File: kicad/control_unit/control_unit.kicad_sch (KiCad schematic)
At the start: 16 parts

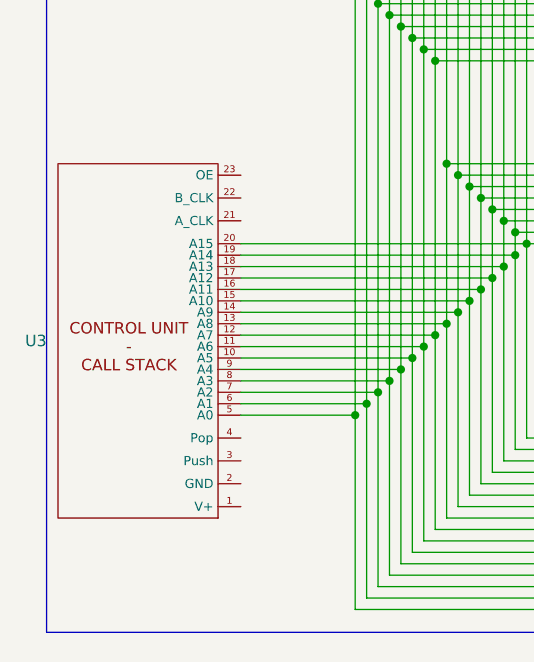
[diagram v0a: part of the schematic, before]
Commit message: Work on call stack and instruction sequence timing
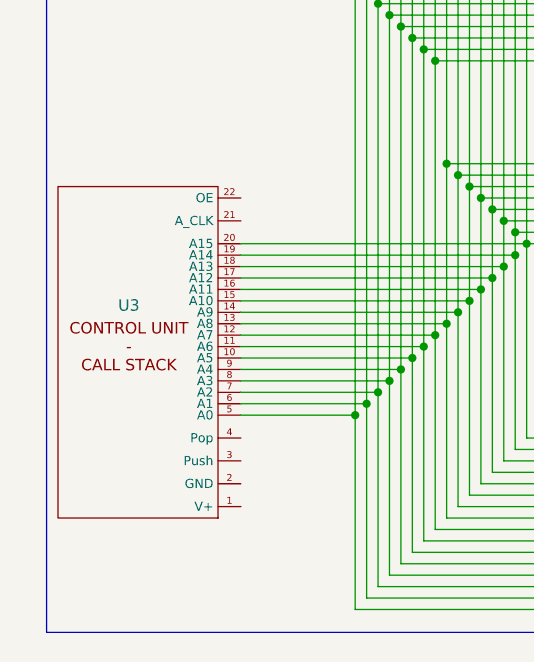
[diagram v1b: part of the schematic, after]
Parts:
- U3: value ~ -> (none); footprint Connector_PinHeader_2.54mm:PinHeader_1x23_P2.54mm_Vertical -> Connector_PinHeader_2.54mm:PinHeader_1x22_P2.54mm_Vertical
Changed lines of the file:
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@@
 		(dnp no)
 		(property "Reference" "U3"
-			(at 138.43 269.8751 0)
+			(at 147.574 265.938 0)
 			(effects
 				(font
 					(size 1.27 1.27)
 				)
-				(justify left)
 			)
 		)
-		(property "Value" "~"
+		(property "Value" ""
 			(at 157.48 275.59 0)
 			(effects
@@
 			)
 		)
-		(property "Footprint" "Connector_PinHeader_2.54mm:PinHeader_1x23_P2.54mm_Vertical"
-			(at 148.336 247.142 0)
+		(property "Footprint" "Connector_PinHeader_2.54mm:PinHeader_1x22_P2.54mm_Vertical"
+			(at 148.336 250.952 0)
 			(effects
 				(font
@@
 		(pin "15"
 		)
-		(pin "23"
-		)
 		(instances

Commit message: Finished startup controller
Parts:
- removed U4: ~, Connector_PinHeader_2.54mm:PinHeader_1x39_P2.54mm_Vertical, symbol custom_symbol_lib:prog_mem_interface
- added D1, D2, D3, D4: LED, LED_THT:LED_D4.0mm, symbol Device:LED
- added R2, R3, R5, R6, R7: 10k, custom_footprint_library:0.4_pitch_resistor, symbol Device:R
- added U11: ~, Connector_PinHeader_2.54mm:PinHeader_1x23_P2.54mm_Horizontal, symbol custom_symbol_lib:control_unit_central_timing_interface
- added U12, U16: ~, Package_DIP:DIP-14_W7.62mm, symbol custom_symbol_lib:quad_and
- added U14: ~, Package_DIP:DIP-14_W7.62mm, symbol custom_symbol_lib:quad_OR
- added U17: ~, Connector_PinHeader_2.54mm:PinHeader_1x40_P2.54mm_Vertical, symbol custom_symbol_lib:prog_mem_interface
- added U20: ~, Package_DIP:DIP-14_W7.62mm, symbol custom_symbol_lib:6xNOT
- added U22: ~, Connector_PinHeader_2.54mm:PinHeader_1x04_P2.54mm_Vertical, symbol custom_symbol_lib:ALU_opcode
- added U23, U25: ~, custom_footprint_library:jumper, symbol custom_symbol_lib:jumper
- added U4: ~, Package_DIP:DIP-14_W7.62mm, symbol custom_symbol_lib:dual_latch
- U1: footprint Connector_PinHeader_2.54mm:PinHeader_1x22_P2.54mm_Vertical -> Connector_PinHeader_2.54mm:PinHeader_1x23_P2.54mm_Vertical
- U2: footprint Connector_PinHeader_2.54mm:PinHeader_1x10_P2.54mm_Vertical -> Connector_PinHeader_2.54mm:PinHeader_1x11_P2.54mm_Vertical
- U3: value (none) -> ~; footprint Connector_PinHeader_2.54mm:PinHeader_1x22_P2.54mm_Vertical -> Connector_PinHeader_2.54mm:PinHeader_1x24_P2.54mm_Vertical
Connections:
- net at U5.1 (OE#): now also U7.1 (OE#), U20.10 (O4)
- net at U5.10 (GND): now also U1.13 (GND), U10.10 (B2), U10.13 (B3), U10.15 (OE#), U10.8 (GND), U13.11 (B3), U13.15 (B2), U13.2 (B1), U13.6 (B0), U13.8 (GND), U15.8 (GND), U18.11 (B3), U18.15 (B2), U18.2 (B1), U18.6 (B0), U18.8 (GND), U19.10 (GND), U21.11 (B3), U21.15 (B2), U21.2 (B1), U21.7 (C_IN), U21.8 (GND), U24.10 (GND), U3.2 (GND), U6.1 (OE#), U6.10 (GND), U7.10 (GND), U8.10 (GND), U9.1 (OE#), U9.10 (GND), D1.1 (K), D2.1 (K), D3.1 (K), D4.1 (K), R2.2, R3.2, R5.2, R6.2, R7.2, U11.2 (GND), U12.7 (GND), U14.1 (0A), U14.2 (0B), U14.5 (1A), U14.6 (1B), U14.7 (GND), U14.8 (2A), U14.9 (2B), U16.7 (GND), U17.2 (GND), U17.4 (W/R#_select), U20.1 (I0), U20.3 (I1), U20.5 (I2), U20.7 (GND), U23.2 (GND), U25.2 (GND), U4.10 (1RESET), U4.11 (1CLK), U4.4 (0RESET), U4.6 (0SET), U4.7 (GND), U4.8 (1SET), U4.9 (1D)
- net at U5.11 (CLK): now also U16.6 (2Q)
- net at U19.12 (Q7), U3.20 (A15), U5.12 (Q7)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: now also U17.23 (A15)
- net at U19.13 (Q6), U3.19 (A14), U5.13 (Q6)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: now also U17.22 (A14)
- net at U19.14 (Q5), U3.18 (A13), U5.14 (Q5)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: now also U17.21 (A13)
- net at U19.15 (Q4), U3.17 (A12), U5.15 (Q4)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: now also U17.20 (A12)
- net at U19.16 (Q3), U3.16 (A11), U5.16 (Q3)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: now also U17.19 (A11)
- net at U19.17 (Q2), U3.15 (A10), U5.17 (Q2)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: now also U17.18 (A10)
- net at U19.18 (Q1), U3.14 (A9), U5.18 (Q1)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: now also U17.17 (A9)
- net at U19.19 (Q0), U3.13 (A8), U5.19 (Q0)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: now also U17.16 (A8)
- net at U1.14 (D0), U5.2 (D0), U7.2 (D0)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: now also U11.11 (BUS-0)
- net at U5.20 (V+): now also U1.12 (V+), U10.16 (V+), U10.3 (B0), U10.6 (B1), U13.16 (V+), U15.16 (V+), U18.16 (V+), U19.20 (V+), U21.16 (V+), U21.6 (B0), U24.20 (V+), U3.1 (V+), U6.20 (V+), U7.20 (V+), U8.20 (V+), U9.20 (V+), U11.1 (V+), U12.14 (V+), U14.14 (V+), U16.14 (V+), U17.1 (V+), U17.7 (OE), U20.14 (V+), U4.14 (V+)
- net at U7.11 (CLK): now also U16.3 (1Q)
- net at U24.12 (Q7), U3.12 (A7), U6.9 (D7)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: now also U17.15 (A7)
- net at U24.13 (Q6), U3.11 (A6), U6.8 (D6)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: now also U17.14 (A6)
- net at U24.14 (Q5), U3.10 (A5), U6.7 (D5)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: now also U17.13 (A5)
- net at U24.15 (Q4), U3.9 (A4), U6.6 (D4)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: now also U17.12 (A4)
- net at U24.16 (Q3), U3.8 (A3), U6.5 (D3)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: now also U17.11 (A3)
- net at U24.17 (Q2), U3.7 (A2), U6.4 (D2)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: now also U17.10 (A2)
- net at U24.18 (Q1), U3.6 (A1), U6.3 (D1)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: now also U17.9 (A1)
- net at U24.19 (Q0), U3.5 (A0), U6.2 (D0)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: now also U17.8 (A0)
- net at U19.1 (OE#), U24.1 (OE#): now also U20.12 (O5)
- net at U19.11 (CLK), U24.11 (CLK): now also U11.16 (POST_ADDER_LATCH_CLOCK)
- net at U1.1 (READ_0): now also R5.1, U16.2 (1B)
- net at U1.10 (CLK_A): now also U3.21 (A_CLK), U11.3 (A_CLK), U16.1 (1A), U16.4 (2A), U17.3 (CLK)
- net at U1.11 (CLK_B): now also U3.22 (B_CLK), U11.4 (B_CLK), U4.3 (0CLK)
- net at U1.2 (READ_1): now also R6.1, U16.5 (2B)
- net at U1.22 (FAULT): now also U14.11 (Q3)
- net at U1.3 (READ_2): now also R7.1, U11.13 (BUS_READ_GOTO-DECIDER)
- net at U1.5 (WRITE_0): now also R3.1, U16.13 (3A)
- net at U1.9 (READ_READY): now also U8.11 (CLK), U20.9 (I3), U25.3 (OUT)
- net at U3.3 (Push): now also U11.20 (CALL_STACK-PUSH)
- net at U3.4 (Pop): now also U11.21 (CALL_STACK-POP)
- net at U8.2 (D0): now also U17.28 (D4), U22.1 (0)
- net at U8.3 (D1): now also U17.29 (D5), U22.2 (1)
- net at U8.4 (D2): now also U17.30 (D6), U22.3 (2)
- net at U8.5 (D3): now also U17.31 (D7), U22.4 (3)
- net at U10.2 (A0), U8.6 (D4): now also U17.32 (D8)
- net at U10.5 (A1), U8.7 (D5): now also U17.33 (D9)
- net at U10.11 (A2), U8.8 (D6): now also U17.34 (D10)
- net at U10.14 (A3), U8.9 (D7): now also U17.35 (D11)
- net at U2.7 (RA0): now also U17.36 (D12)
- net at U2.8 (RA1): now also U17.37 (D13)
- net at U2.9 (RA2): now also U17.38 (D14)
- net at U2.10 (RA3): now also U17.39 (D15)
- net at U8.1 (OE#): now also U20.8 (03)
- net at U2.1 (Move): now also U11.14 (BUS_MOVE)
- net at U2.2 (Done): now also U11.5 (BUS_MOVE_DONE)
- net at U10.1 (S): now also D4.2 (A), U11.7 (INSTRUCTION-0), U17.24 (D0)
- net at U6.11 (CLK), U9.11 (CLK): now also U11.15 (PRE_ADDER_LATCH_CLOCK)
- new net: D3.2 (A), U11.8 (INSTRUCTION-1), U17.25 (D1)
- new net: D2.2 (A), U11.9 (INSTRUCTION-2), U17.26 (D2)
- new net: D1.2 (A), U11.10 (INSTRUCTION-3), U17.27 (D3)
- new net: R2.1, U1.23 (ENABLE), U12.1 (1A), U12.10 (4A), U12.13 (3A), U12.4 (2A), U16.10 (4A), U17.40 (ENABLE)
- new net: U11.18 (PROG_READ), U17.5 (Start)
- new net: U17.6 (Done), U23.1 (IN)
- new net: U11.19 (FAULT), U14.12 (3A)
- new net: U14.13 (3B), U3.24 (FAULT)
- new net: U16.9 (4B), U4.1 (0Q)
- new net: U16.12 (3B), U4.2 (0Q#)
- new net: U16.11 (3Q), U4.5 (0D)
- new net: U11.12 (START), U2.11 (Start)
- new net: U11.17 (POST_ADDER_LATCH_OE), U12.9 (4B)
- new net: U11.22 (CALL_STACK-OE), U12.2 (1B)
- new net: U11.23 (GOTO_LATCHES_OE), U12.5 (2B)
- new net: U11.6 (PROG_READ_DONE), U12.11 (3Q)
- new net: U12.3 (1Q), U3.23 (OE)
- new net: U12.6 (2Q), U20.11 (I4)
- new net: U12.8 (4Q), U20.13 (I5)
- new net: U12.12 (3B), U23.3 (OUT)
- new net: U16.8 (4Q), U25.1 (IN)
- no-connect marks 1 -> 13
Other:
- note added: "CALL STACK OE"
- note added: "GOTO OE ->"
- note added: "GOTO-A"
- note added: "GOTO-B"
- note added: "Prog read done"
- moved on the sheet: U10, U13, U15, U18, U19, U21, U24, U5, U6, U7, U8, U9

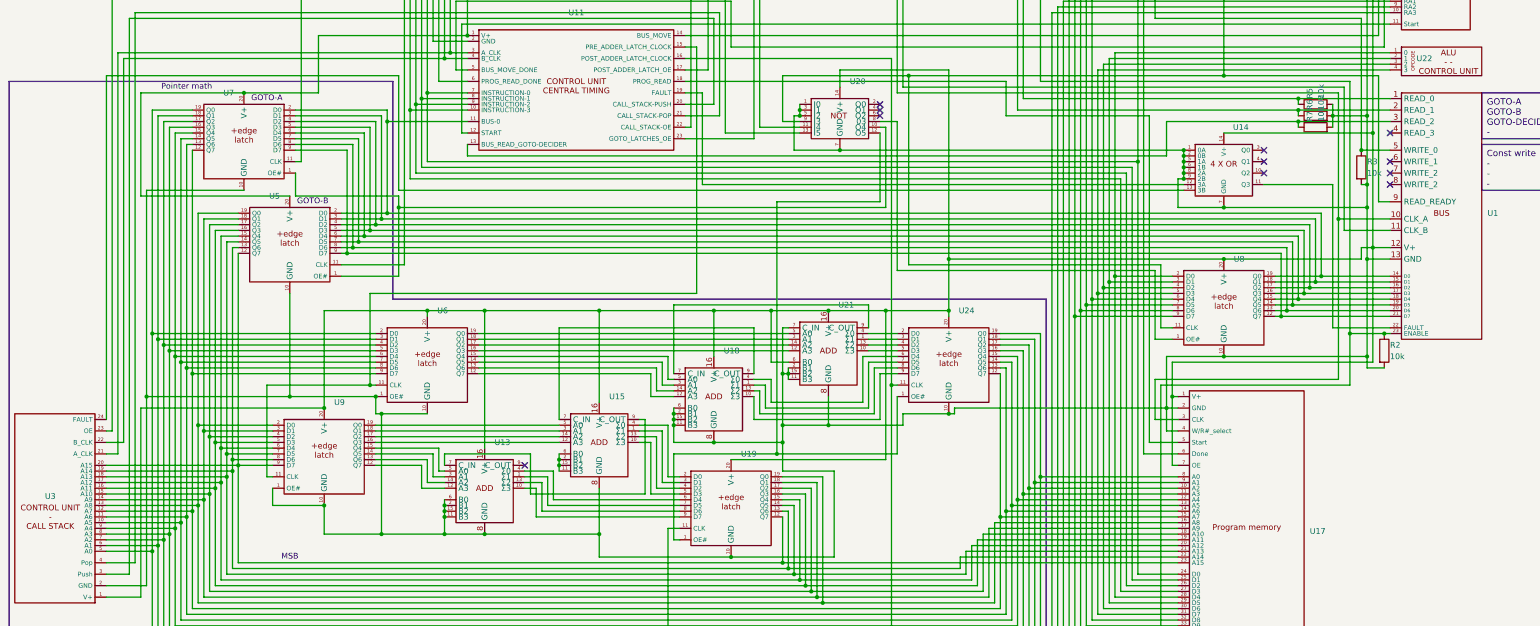
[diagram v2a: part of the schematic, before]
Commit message: Added pullup resistors to control unit memory address
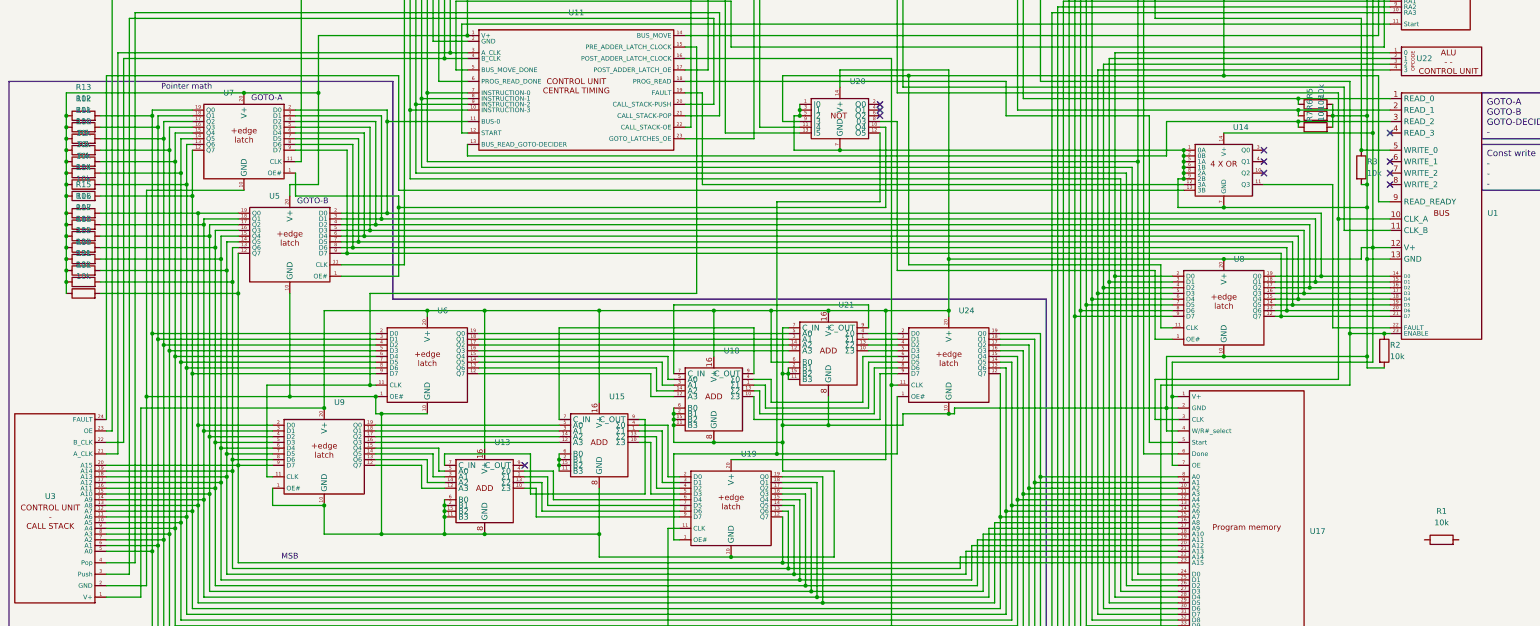
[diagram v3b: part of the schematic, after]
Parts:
- added R1, R10, R11, R12, R13, R14, R15, R16, R17, R18, R19, R20, R21, R22, R4, R8, R9: 10k, custom_footprint_library:0.4_pitch_resistor, symbol Device:R
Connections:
- net at U1.12 (V+), U10.16 (V+), U10.3 (B0)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: now also R10.1, R11.1, R12.1, R13.1, R14.1, R15.1, R16.1, R17.1, R18.1, R19.1, R20.1, R21.1, R22.1, R4.1, R8.1, R9.1
- net at U17.10 (A2), U24.17 (Q2), U3.7 (A2)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: now also R11.2
- net at U17.11 (A3), U24.16 (Q3), U3.8 (A3)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: now also R10.2
- net at U17.12 (A4), U24.15 (Q4), U3.9 (A4)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: now also R9.2
- net at U17.13 (A5), U24.14 (Q5), U3.10 (A5)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: now also R8.2
- net at U17.14 (A6), U24.13 (Q6), U3.11 (A6)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: now also R4.2
- net at U17.15 (A7), U24.12 (Q7), U3.12 (A7)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: now also R14.2
- net at U17.16 (A8), U19.19 (Q0), U3.13 (A8)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: now also R15.2
- net at U17.17 (A9), U19.18 (Q1), U3.14 (A9)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: now also R16.2
- net at U17.18 (A10), U19.17 (Q2), U3.15 (A10)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: now also R17.2
- net at U17.19 (A11), U19.16 (Q3), U3.16 (A11)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: now also R18.2
- net at U17.20 (A12), U19.15 (Q4), U3.17 (A12)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: now also R19.2
- net at U17.21 (A13), U19.14 (Q5), U3.18 (A13)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: now also R20.2
- net at U17.22 (A14), U19.13 (Q6), U3.19 (A14)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: now also R21.2
- net at U17.23 (A15), U19.12 (Q7), U3.20 (A15)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: now also R22.2
- net at U17.8 (A0), U24.19 (Q0), U3.5 (A0)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: now also R13.2
- net at U17.9 (A1), U24.18 (Q1), U3.6 (A1)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: now also R12.2

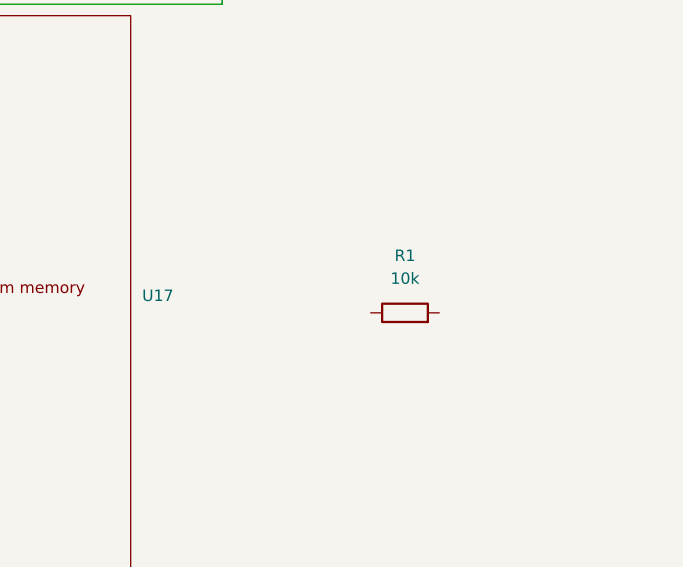
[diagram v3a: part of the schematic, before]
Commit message: Working on GPRAM schematic
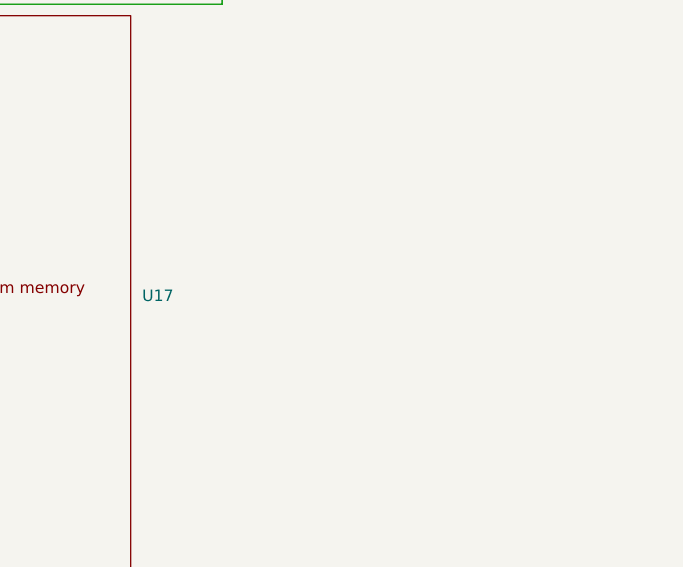
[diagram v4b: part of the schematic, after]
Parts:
- removed R1: 10k, custom_footprint_library:0.4_pitch_resistor, symbol Device:R
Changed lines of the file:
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@@
-	(symbol
-		(lib_id "Device:R")
-		(at 359.41 215.9 90)
-		(unit 1)
-		(exclude_from_sim no)
-		(in_bom yes)
-		(on_board yes)
-		(dnp no)
-		(fields_autoplaced yes)
-		(property "Reference" "R1"
-			(at 359.41 209.55 90)
-			(effects
-				(font
-					(size 1.27 1.27)
-				)
-			)
-		)
-		(property "Value" "10k"
-			(at 359.41 212.09 90)
-			(effects
-				(font
-					(size 1.27 1.27)
-				)
-			)
-		)
-		(property "Footprint" "custom_footprint_library:0.4_pitch_resistor"
-			(at 359.41 217.678 90)
-			(effects
-				(font
-					(size 1.27 1.27)
-				)
-				(hide yes)
-			)
-		)
-		(property "Datasheet" "~"
-			(at 359.41 215.9 0)
-			(effects
-				(font
-					(size 1.27 1.27)
-				)
-				(hide yes)
-			)
-		)
-		(property "Description" "Resistor"
-			(at 359.41 215.9 0)
-			(effects
-				(font
-					(size 1.27 1.27)
-				)
-				(hide yes)
-			)
-		)
-		(pin "1"
-		)
-		(pin "2"
-		)
-		(instances
-			(project "control_unit"
-				(path "/a283fd53-b6aa-4802-95bb-5cb867d300d3"
-					(reference "R1")
-					(unit 1)
-				)
-			)
-		)
-	)
 	(symbol
 		(lib_id "Device:R")

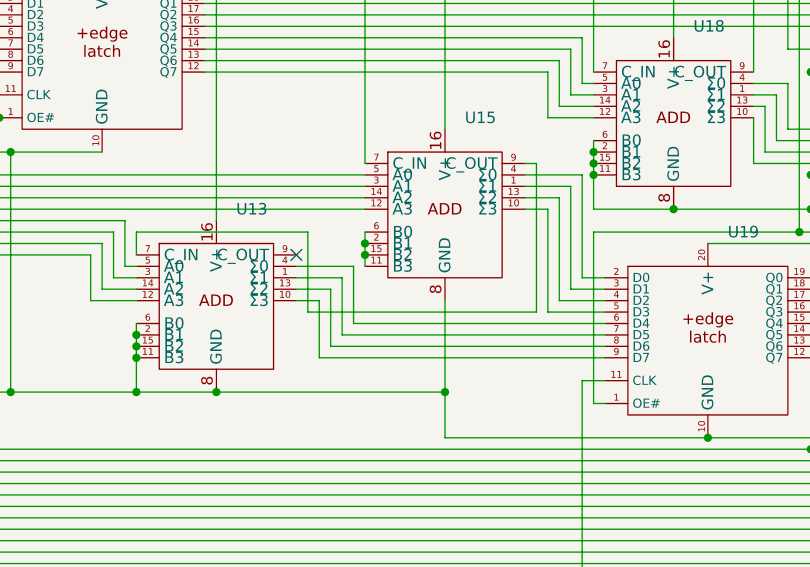
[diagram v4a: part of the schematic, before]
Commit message: Finished call stack schematic
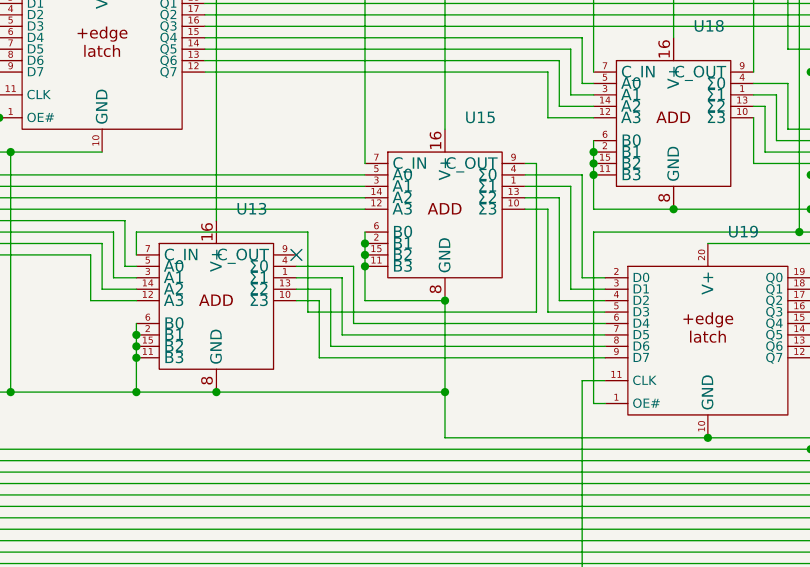
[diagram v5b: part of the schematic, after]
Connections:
- net at D1.1 (K), D2.1 (K), D3.1 (K)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: now also U15.11 (B3), U15.15 (B2), U15.2 (B1), U15.6 (B0)
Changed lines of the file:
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@@
 	(paper "A3")
 	(junction
+		(at 172.72 204.47)
+		(diameter 0)
+		(color 0 0 0 0)
+	)
+	(junction
 		(at 223.52 83.82)
 		(diameter 0)
@@
 	)
 	(junction
+		(at 163.83 200.66)
+		(diameter 0)
+		(color 0 0 0 0)
+	)
+	(junction
 		(at 298.45 186.69)
 		(diameter 0)
@@
 	(wire
 		(pts
+			(xy 163.83 204.47) (xy 172.72 204.47)
+		)
+		(stroke
+			(width 0)
+			(type default)
+		)
+	)
+	(wire
+		(pts
 			(xy 76.2 127) (xy 76.2 172.72)
 		)
@@
 		)
 		(stroke
+			(width 0)
+			(type default)
+		)
+	)
+	(wire
+		(pts
+			(xy 163.83 200.66) (xy 163.83 204.47)
+		)
+		(stroke
